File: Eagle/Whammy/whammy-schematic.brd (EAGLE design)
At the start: 160 x 100 mm, 16 parts, among them J1 POWER_JACK, J2 DIN5, J3 UP, J4 DOWN, J5 GND, J6 5V, J7 9V, J8 3P3V, U1 5V REGULATOR

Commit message: Added initial layout. No ground fill yet.
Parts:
- removed J5: GND, SparkFun-Connectors:1X01
- removed J6: 5V, SparkFun-Connectors:1X01
- removed J7: 9V, SparkFun-Connectors:1X01
- removed J8: 3P3V, SparkFun-Connectors:1X01
- added H1, H2, H3, H4: STAND-OFF, SparkFun-Hardware:STAND-OFF
- added J9: (no value), SparkFun-Connectors:1X04
- moved R2 160.7 mm to (83.8, 31.8), turned to 180 degrees
- moved R1 155.7 mm to (85.1, 21.6)
- moved J4 134.2 mm to (61.0, 7.62)
- moved J3 118.6 mm to (48.3, 7.62)
- moved J2 113.7 mm to (110.5, 20.3), turned to 90 degrees
- moved LCD1 109.2 mm to (55.9, 20.3), flipped to the bottom
- moved U1 98.4 mm to (16.5, 14.0), turned to 90 degrees
- moved C1 76.1 mm to (17.8, 24.1), turned to 270 degrees
- moved J1 62.9 mm to (0.00, 27.9), turned to 270 degrees
- moved VR1 50.8 mm to (80.0, 12.7), turned to 180 degrees
- moved U$1 39.6 mm to (53.3, 22.9)
- moved C2 34.7 mm to (27.9, 22.9)
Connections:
- net 3P3V: now also J9.3; no longer J8.1
- net 5V: now also J9.2; no longer J6.1
- net 9V: now also J9.1; no longer J7.1
- net GND: now also J9.4; no longer J5.1
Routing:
- net 5V: track 0.00 -> 147.9 mm
- net 3P3V: track 0.00 -> 69.6 mm
- net 9V: track 0.00 -> 47.5 mm
- net MIDIOUT: track 0.00 -> 42.0 mm
- net VO: track 0.00 -> 26.2 mm
- net DOWN: track 0.00 -> 17.1 mm
- net RS: track 0.00 -> 15.2 mm
- net E: track 0.00 -> 13.4 mm
- net N$2: track 0.00 -> 10.5 mm
- net UP: track 0.00 -> 9.20 mm
- net N$1: track 0.00 -> 9.19 mm
- net DB7: track 0.00 -> 5.44 mm
- net DB6: track 0.00 -> 5.44 mm
- net DB5: track 0.00 -> 5.44 mm
- net DB4: track 0.00 -> 5.44 mm
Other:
- board size 160 x 100 mm -> 110.5 x 41.9 mm
- board text added: "3P3V"
- board text added: "5V"
- board text added: "9V"
- board text added: "GND"
- board text added: "Ryan S. Frankel"
- board text added: "WHAM CONTROL"
- board text added: "v0.1"

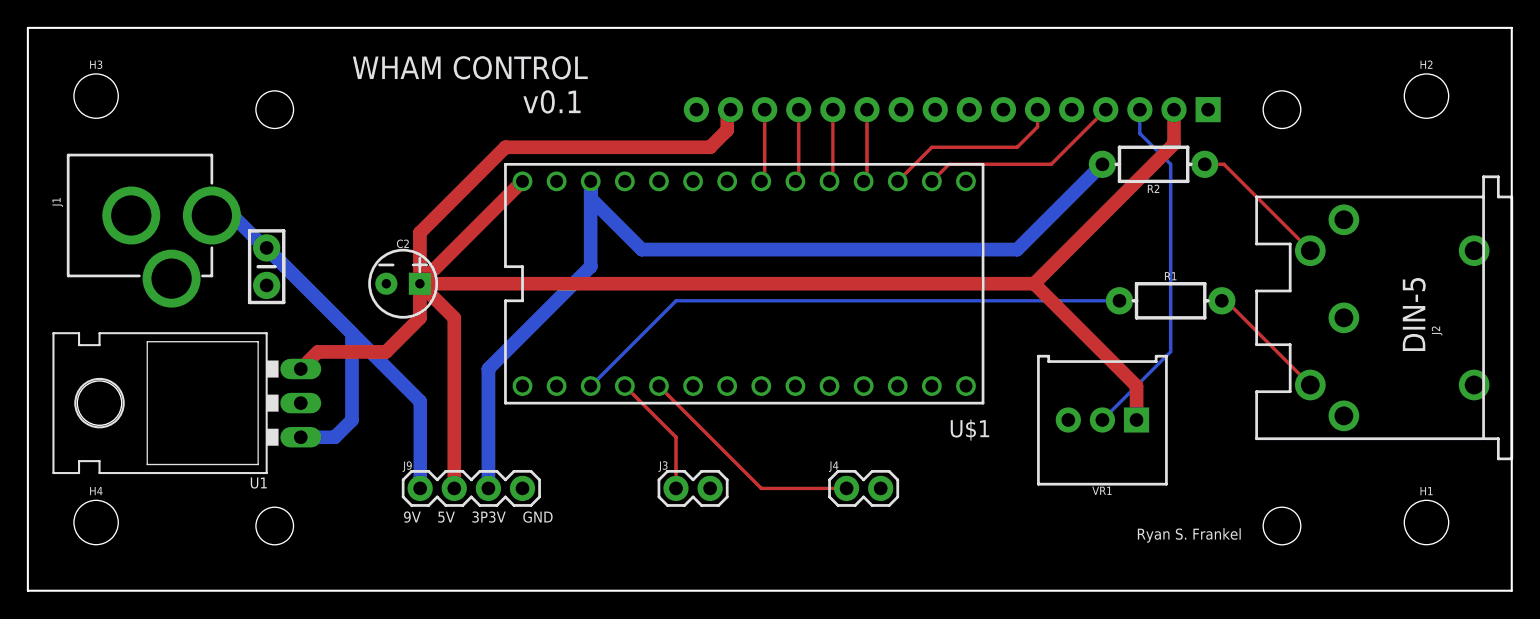
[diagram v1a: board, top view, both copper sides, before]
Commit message: Finished board with planes. Including OSHPark design rules file.
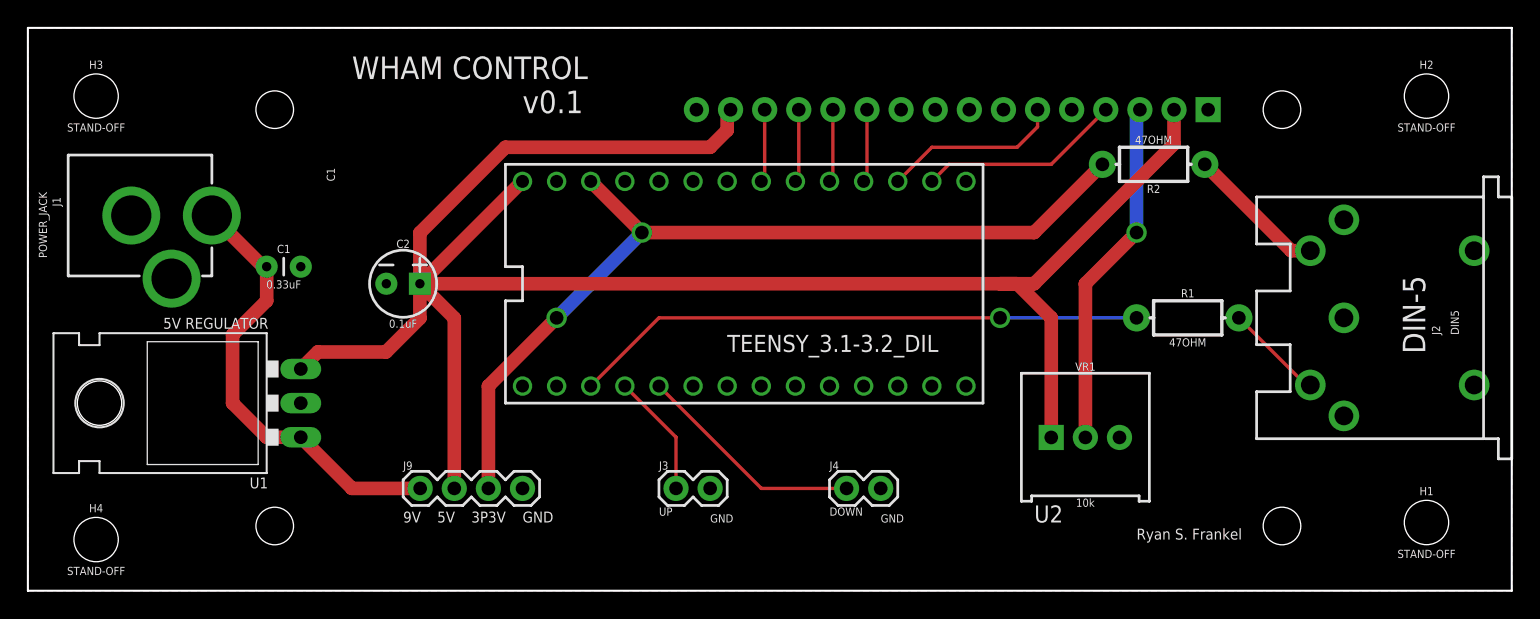
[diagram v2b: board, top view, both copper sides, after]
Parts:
- C1: device SparkFun-Capacitors:CAP-PTH-SMALL-KIT -> SparkFun-Capacitors:CAP-PTH-2.54
- moved VR1 1.80 mm to (78.7, 11.4), turned to 0 degrees
- moved R1 1.80 mm to (86.4, 20.3)
- moved H4 1.27 mm to (5.08, 3.81)
- moved C1 1.27 mm to (19.1, 24.1), turned to 0 degrees
- renumbered U$1 to U2
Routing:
- net 9V: track 47.5 -> 33.5 mm
- net 3P3V: track 69.6 -> 65.6 mm, vias 0 -> 2
- net N$1: track 9.19 -> 7.39 mm
- net MIDIOUT: track 42.0 -> 42.7 mm, vias 0 -> 1
- net VO: track 26.2 -> 26.1 mm, vias 0 -> 1
- added copper zone on layer 1, net GND
- added copper zone on layer 16, net N$3
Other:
- board text added: "1"
- board text added: "C1"
